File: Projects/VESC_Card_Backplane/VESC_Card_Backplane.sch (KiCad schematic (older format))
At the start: 1 part

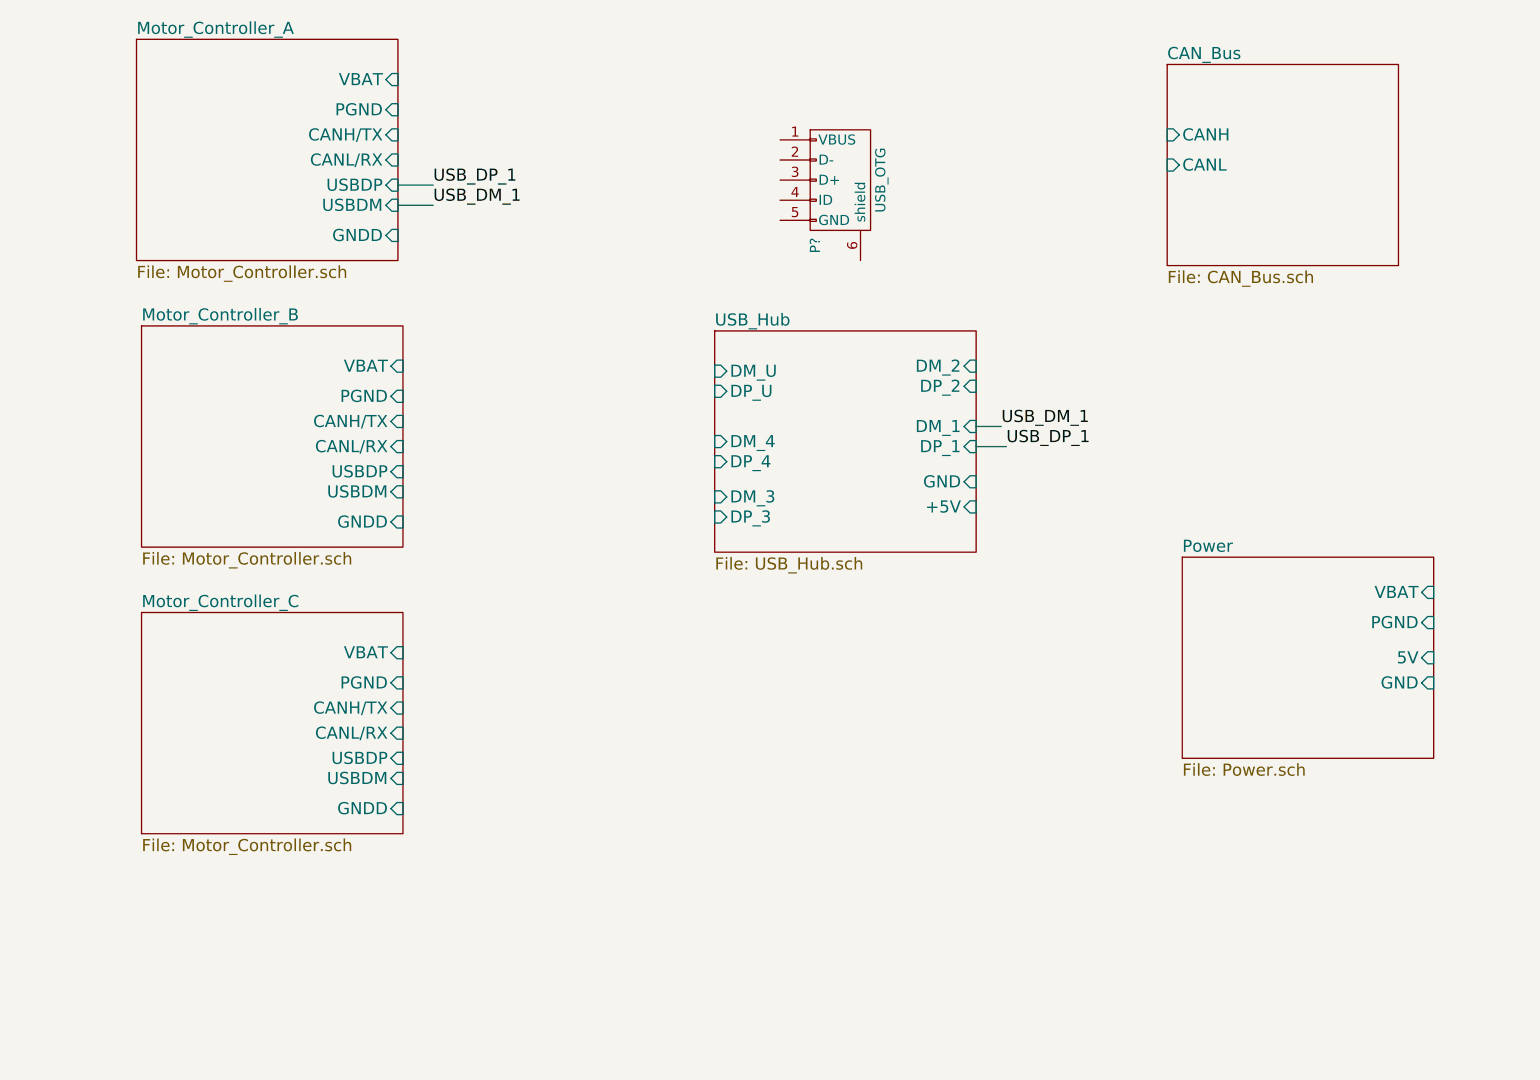
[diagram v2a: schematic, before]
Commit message: Connected subsheets on eeschema
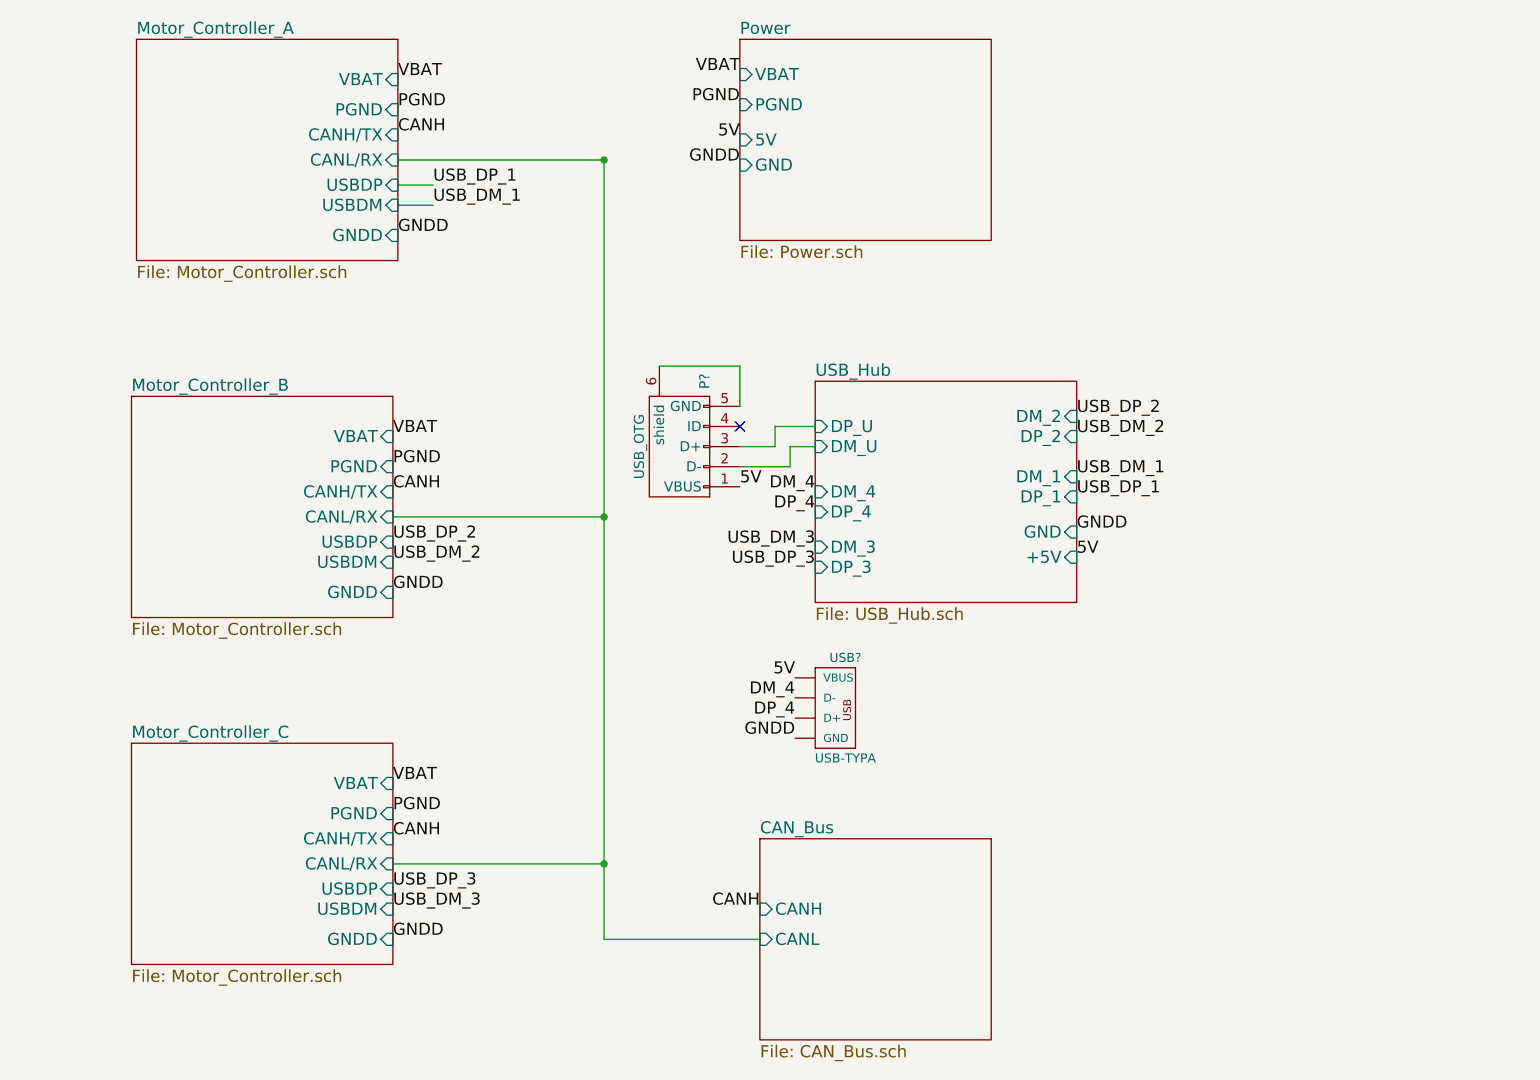
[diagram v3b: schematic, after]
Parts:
- added USB?: USB-TYPA, USB-A-F-PTH, symbol USB-TYPA
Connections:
- net USB_Hub/DM_U: now also P?.2 (D-)
- net USB_Hub/DP_U: now also P?.3 (D+)
- net 5V: now reaches P?.1 (VBUS)
- net 5V: now also USB?.VBUS
- net at P?.5 (GND): now also P?.6 (shield)
- new net DM_4: USB?.D-
- new net DP_4: USB?.D+
- new net GNDD: USB?.GND
- no-connect marks 0 -> 1
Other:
- moved on the sheet: P?
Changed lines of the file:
@@
 $Descr A4 11693 8268
 encoding utf-8
-Sheet 1 6
+Sheet 1 7
 Title ""
 Date ""
@@
 $EndDescr
 $Sheet
-S 4325 2550 1300 1100
+S 4825 2800 1300 1100
 U 5871A1CF
 F0 "USB_Hub" 60
 F1 "USB_Hub.sch" 60
-F2 "DM_U" I L 4325 2750 60
-F3 "DP_U" I L 4325 2850 60
-F4 "DM_4" I L 4325 3100 60
-F5 "DP_4" I L 4325 3200 60
-F6 "DM_3" I L 4325 3375 60
-F7 "DP_3" I L 4325 3475 60
-F8 "DM_2" I R 5625 2725 60
-F9 "DP_2" I R 5625 2825 60
-F10 "DM_1" I R 5625 3025 60
-F11 "DP_1" I R 5625 3125 60
-F12 "GND" I R 5625 3300 60
-F13 "+5V" I R 5625 3425 60
+F2 "DM_U" I L 4825 3125 60
+F3 "DP_U" I L 4825 3025 60
+F4 "DM_4" I L 4825 3350 60
+F5 "DP_4" I L 4825 3450 60
+F6 "DM_3" I L 4825 3625 60
+F7 "DP_3" I L 4825 3725 60
+F8 "DM_2" I R 6125 2975 60
+F9 "DP_2" I R 6125 3075 60
+F10 "DM_1" I R 6125 3275 60
+F11 "DP_1" I R 6125 3375 60
+F12 "GND" I R 6125 3550 60
+F13 "+5V" I R 6125 3675 60
 $EndSheet
 $Sheet
@@
 $EndSheet
 $Sheet
-S 6650 3675 1250 1000
+S 4450 1100 1250 1000
 U 5871DB4E
 F0 "Power" 60
 F1 "Power.sch" 60
-F2 "VBAT" I R 7900 3850 60
-F3 "PGND" I R 7900 4000 60
-F4 "5V" I R 7900 4175 60
-F5 "GND" I R 7900 4300 60
-$EndSheet
-$Sheet
-S 6575 1225 1150 1000
+F2 "VBAT" I L 4450 1275 60
+F3 "PGND" I L 4450 1425 60
+F4 "5V" I L 4450 1600 60
+F5 "GND" I L 4450 1725 60
+$EndSheet
+$Sheet
+S 4550 5075 1150 1000
 U 5871E13C
 F0 "CAN_Bus" 60
 F1 "CAN_Bus.sch" 60
-F2 "CANH" I L 6575 1575 60
-F3 "CANL" I L 6575 1725 60
-$EndSheet
-$Sheet
-S 1475 2525 1300 1100
+F2 "CANH" I L 4550 5425 60
+F3 "CANL" I L 4550 5575 60
+$EndSheet
+$Sheet
+S 1425 2875 1300 1100
 U 5878CF59
 F0 "Motor_Controller_B" 60
 F1 "Motor_Controller.sch" 60
-F2 "VBAT" I R 2775 2725 60
-F3 "PGND" I R 2775 2875 60
-F4 "CANH/TX" I R 2775 3000 60
-F5 "CANL/RX" I R 2775 3125 60
-F6 "USBDP" I R 2775 3250 60
-F7 "USBDM" I R 2775 3350 60
-F8 "GNDD" I R 2775 3500 60
-$EndSheet
-$Sheet
-S 1475 3950 1300 1100
+F2 "VBAT" I R 2725 3075 60
+F3 "PGND" I R 2725 3225 60
+F4 "CANH/TX" I R 2725 3350 60
+F5 "CANL/RX" I R 2725 3475 60
+F6 "USBDP" I R 2725 3600 60
+F7 "USBDM" I R 2725 3700 60
+F8 "GNDD" I R 2725 3850 60
+$EndSheet
+$Sheet
+S 1425 4600 1300 1100
 U 5878D5C8
 F0 "Motor_Controller_C" 60
 F1 "Motor_Controller.sch" 60
-F2 "VBAT" I R 2775 4150 60
-F3 "PGND" I R 2775 4300 60
-F4 "CANH/TX" I R 2775 4425 60
-F5 "CANL/RX" I R 2775 4550 60
-F6 "USBDP" I R 2775 4675 60
-F7 "USBDM" I R 2775 4775 60
-F8 "GNDD" I R 2775 4925 60
-$EndSheet
-Wire Wire Line
-	2750 1825 2925 1825
-Wire Wire Line
-	2750 1925 2925 1925
+F2 "VBAT" I R 2725 4800 60
+F3 "PGND" I R 2725 4950 60
+F4 "CANH/TX" I R 2725 5075 60
+F5 "CANL/RX" I R 2725 5200 60
+F6 "USBDP" I R 2725 5325 60
+F7 "USBDM" I R 2725 5425 60
+F8 "GNDD" I R 2725 5575 60
+$EndSheet
 Text Label 2925 1825 0    60   ~ 0
 USB_DP_1
 Text Label 2925 1925 0    60   ~ 0
 USB_DM_1
-Wire Wire Line
-	5625 3125 5775 3125
-Text Label 5775 3125 0    60   ~ 0
+Text Label 6125 3375 0    60   ~ 0
 USB_DP_1
-Wire Wire Line
-	5625 3025 5750 3025
-Text Label 5750 3025 0    60   ~ 0
+Text Label 6125 3275 0    60   ~ 0
 USB_DM_1
 $Comp
 L USB_OTG P?
 U 1 1 58790821
-P 4950 1800
-F 0 "P?" H 5275 1675 50  0000 C CNN
-F 1 "USB_OTG" H 4950 2000 50  0000 C CNN
-F 2 "" V 4900 1700 50  0000 C CNN
-F 3 "" V 4900 1700 50  0000 C CNN
-	1    4950 1800
-	0    1    1    0
+P 4150 3125
+F 0 "P?" H 4475 3000 50  0000 C CNN
+F 1 "USB_OTG" H 4150 3325 50  0000 C CNN
+F 2 "" V 4100 3025 50  0000 C CNN
+F 3 "" V 4100 3025 50  0000 C CNN
+	1    4150 3125
+	0    -1   -1   0
 $EndComp
+Text Label 2725 3600 0    60   ~ 0
+USB_DP_2
+Text Label 2725 3700 0    60   ~ 0
+USB_DM_2
+Text Label 6125 2975 0    60   ~ 0
+USB_DP_2
+Text Label 6125 3075 0    60   ~ 0
+USB_DM_2
+Text Label 2725 5325 0    60   ~ 0
+USB_DP_3
+Text Label 4825 3725 2    60   ~ 0
+USB_DP_3
+Text Label 4825 3625 2    60   ~ 0
+USB_DM_3
+Text Label 2750 1300 0    60   ~ 0
+VBAT
+Text Label 4450 1275 2    60   ~ 0
+VBAT
+Text Label 2725 3075 0    60   ~ 0
+VBAT
+Text Label 2725 4800 0    60   ~ 0
+VBAT
+Text Label 2725 5425 0    60   ~ 0
+USB_DM_3
+Text Label 2750 2075 0    60   ~ 0
+GNDD
+Text Label 2725 3850 0    60   ~ 0
+GNDD
+Text Label 2725 5575 0    60   ~ 0
+GNDD
+Text Label 6125 3550 0    60   ~ 0
+GNDD
+Text Label 2750 1450 0    60   ~ 0
+PGND
+Text Label 2725 3225 0    60   ~ 0
+PGND
+Text Label 2725 4950 0    60   ~ 0
+PGND
+Text Label 4450 1425 2    60   ~ 0
+PGND
+Text Label 4450 1725 2    60   ~ 0
+GNDD
+Text Label 4450 1600 2    60   ~ 0
+5V
+Text Label 6125 3675 0    60   ~ 0
+5V
+$Comp
+L USB-TYPA USB?
+U 1 1 5878FC25
+P 4975 4425
+F 0 "USB?" H 4975 4675 45  0000 C CNN
+F 1 "USB-TYPA" H 4975 4175 45  0000 C CNN
+F 2 "USB-A-F-PTH" H 4975 4125 20  0001 C CNN
+F 3 "" H 4975 4425 60  0000 C CNN
+	1    4975 4425
+	1    0    0    -1
+$EndComp
+Text Label 4825 3350 2    60   ~ 0
+DM_4
+Text Label 4825 3450 2    60   ~ 0
+DP_4
+Text Label 4725 4375 2    60   ~ 0
+DM_4
+Text Label 4725 4475 2    60   ~ 0
+DP_4
+Wire Wire Line
+	2750 1825 2925 1825
+Wire Wire Line
+	2750 1925 2925 1925
+Wire Wire Line
+	2750 1700 3775 1700
+Connection ~ 3775 1700
+Wire Wire Line
+	3775 5575 4550 5575
+Wire Wire Line
+	2725 5200 3775 5200
+Connection ~ 3775 5200
+Wire Wire Line
+	2725 3475 3775 3475
+Connection ~ 3775 3475
+Wire Wire Line
+	4050 2725 4450 2725
+Wire Wire Line
+	4450 2725 4450 2925
+Wire Wire Line
+	4450 3125 4625 3125
+Wire Wire Line
+	4625 3125 4625 3025
+Wire Wire Line
+	4625 3025 4825 3025
+Wire Wire Line
+	4450 3225 4700 3225
+Wire Wire Line
+	4700 3225 4700 3125
+Wire Wire Line
+	4700 3125 4825 3125
+Wire Wire Line
+	3775 1700 3775 5575
+NoConn ~ 4450 3025
+Text Label 4550 5425 2    60   ~ 0
+CANH
+Text Label 2725 5075 0    60   ~ 0
+CANH
+Text Label 2725 3350 0    60   ~ 0
+CANH
+Text Label 2750 1575 0    60   ~ 0
+CANH
+Text Label 4725 4275 2    60   ~ 0
+5V
+Text Label 4725 4575 2    60   ~ 0
+GNDD
+Text Label 4450 3325 0    60   ~ 0
+5V
 $EndSCHEMATC

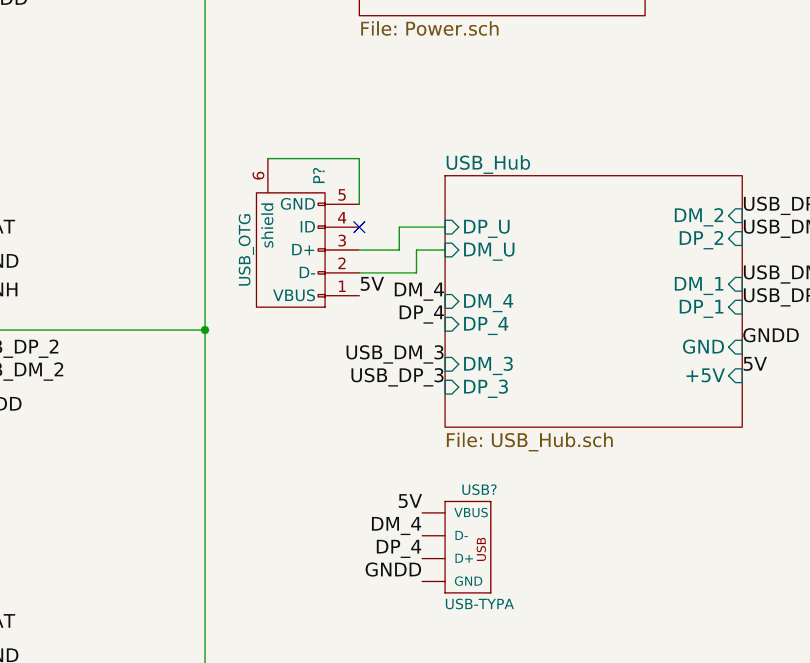
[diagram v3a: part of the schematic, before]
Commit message: Footprint assoc. for backplane
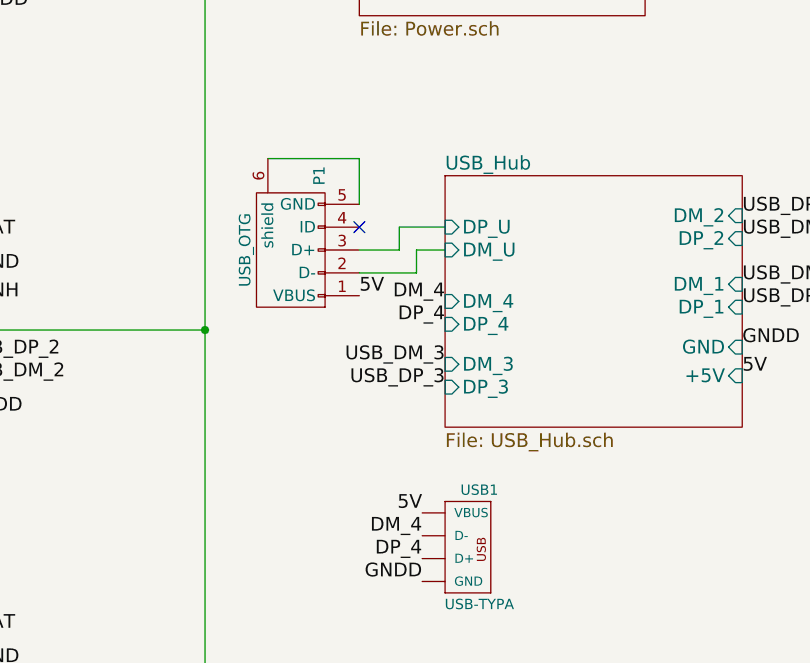
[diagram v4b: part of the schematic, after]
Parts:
- P1: renamed from P?; footprint (none) -> Connectors:USB_Mini-B
- USB1: renamed from USB?; footprint USB-A-F-PTH -> USST-footprints:USB_A_PTH_AMP787616-1
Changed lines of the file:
@@
 USB_DM_1
 $Comp
-L USB_OTG P?
+L USB_OTG P1
 U 1 1 58790821
 P 4150 3125
-F 0 "P?" H 4475 3000 50  0000 C CNN
+F 0 "P1" H 4475 3000 50  0000 C CNN
 F 1 "USB_OTG" H 4150 3325 50  0000 C CNN
-F 2 "" V 4100 3025 50  0000 C CNN
+F 2 "Connectors:USB_Mini-B" V 4100 3025 50  0001 C CNN
 F 3 "" V 4100 3025 50  0000 C CNN
 	1    4150 3125
@@
 5V
 $Comp
-L USB-TYPA USB?
+L USB-TYPA USB1
 U 1 1 5878FC25
 P 4975 4425
-F 0 "USB?" H 4975 4675 45  0000 C CNN
+F 0 "USB1" H 4975 4675 45  0000 C CNN
 F 1 "USB-TYPA" H 4975 4175 45  0000 C CNN
-F 2 "USB-A-F-PTH" H 4975 4125 20  0001 C CNN
+F 2 "USST-footprints:USB_A_PTH_AMP787616-1" H 4975 4125 20  0001 C CNN
 F 3 "" H 4975 4425 60  0000 C CNN
 	1    4975 4425
@@
 Wire Wire Line
 	2750 1925 2925 1925
-Wire Wire Line
-	2750 1700 3775 1700
 Connection ~ 3775 1700
 Wire Wire Line
@@
 Text Label 4450 3325 0    60   ~ 0
 5V
+Wire Wire Line
+	2750 1700 3775 1700
 $EndSCHEMATC

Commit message: Comleted VESC Backplane
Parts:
- added JP2: J, USST-footprints:J_0603, symbol Jumper_NO_Small
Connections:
- net 5V: now also JP2.1; no longer P1.1 (VBUS)
- net GNDD: now also P1.5 (GND), P1.6 (shield)
- new net: JP2.2, P1.1 (VBUS)
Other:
- note added: "Note: Due to layout constraints, pgnd = gndd for A and B\n"
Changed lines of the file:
@@
 	0    -1   -1   0
 $EndComp
-Text Label 2725 3600 0    60   ~ 0
+Text Label 2900 3600 0    60   ~ 0
 USB_DP_2
-Text Label 2725 3700 0    60   ~ 0
+Text Label 2900 3700 0    60   ~ 0
 USB_DM_2
+Text Label 6125 3075 0    60   ~ 0
+USB_DP_2
 Text Label 6125 2975 0    60   ~ 0
-USB_DP_2
-Text Label 6125 3075 0    60   ~ 0
 USB_DM_2
-Text Label 2725 5325 0    60   ~ 0
+Text Label 2825 5325 0    60   ~ 0
 USB_DP_3
 Text Label 4825 3725 2    60   ~ 0
@@
 Text Label 2725 4800 0    60   ~ 0
 VBAT
-Text Label 2725 5425 0    60   ~ 0
+Text Label 2825 5425 0    60   ~ 0
 USB_DM_3
-Text Label 2750 2075 0    60   ~ 0
-GNDD
-Text Label 2725 3850 0    60   ~ 0
-GNDD
 Text Label 2725 5575 0    60   ~ 0
 GNDD
@@
 Text Label 4725 4475 2    60   ~ 0
 DP_4
+NoConn ~ 4450 3025
+Text Label 4550 5425 2    60   ~ 0
+CANH
+Text Label 2725 5075 0    60   ~ 0
+CANH
+Text Label 2725 3350 0    60   ~ 0
+CANH
+Text Label 2750 1575 0    60   ~ 0
+CANH
+Text Label 4725 4275 2    60   ~ 0
+5V
+Text Label 4725 4575 2    60   ~ 0
+GNDD
+Text Label 4200 3600 0    60   ~ 0
+5V
+Text Label 4350 2550 2    60   ~ 0
+GNDD
 Wire Wire Line
 	2750 1825 2925 1825
@@
 Wire Wire Line
 	3775 1700 3775 5575
-NoConn ~ 4450 3025
-Text Label 4550 5425 2    60   ~ 0
-CANH
-Text Label 2725 5075 0    60   ~ 0
-CANH
-Text Label 2725 3350 0    60   ~ 0
-CANH
-Text Label 2750 1575 0    60   ~ 0
-CANH
-Text Label 4725 4275 2    60   ~ 0
-5V
-Text Label 4725 4575 2    60   ~ 0
-GNDD
-Text Label 4450 3325 0    60   ~ 0
-5V
 Wire Wire Line
 	2750 1700 3775 1700
+Wire Wire Line
+	4450 2800 4450 2550
+Wire Wire Line
+	4450 2550 4350 2550
+Connection ~ 4450 2800
+$Comp
+L Jumper_NO_Small JP2
+U 1 1 5882581A
+P 4400 3450
+F 0 "JP2" H 4400 3530 50  0000 C CNN
+F 1 "J" H 4410 3390 50  0000 C CNN
+F 2 "USST-footprints:J_0603" H 4400 3450 50  0001 C CNN
+F 3 "" H 4400 3450 50  0000 C CNN
+	1    4400 3450
+	1    0    0    -1
+$EndComp
+Wire Wire Line
+	4450 3325 4550 3325
+Wire Wire Line
+	4550 3325 4550 3450
+Wire Wire Line
+	4550 3450 4500 3450
+Wire Wire Line
+	4300 3450 4200 3450
+Wire Wire Line
+	4200 3450 4200 3600
+Wire Wire Line
+	2900 3600 2725 3600
+Wire Wire Line
+	2900 3700 2725 3700
+Wire Wire Line
+	2825 5325 2725 5325
+Wire Wire Line
+	2825 5425 2725 5425
+Text Label 2800 3850 0    60   ~ 0
+PGND
+Wire Wire Line
+	2800 3850 2725 3850
+Text Label 2750 2075 0    60   ~ 0
+PGND
+Text Notes 850  2600 0    60   ~ 0
+Note: Due to layout constraints, pgnd = gndd for A and B\n
 $EndSCHEMATC
